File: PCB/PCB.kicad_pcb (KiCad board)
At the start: 2 copper layers, 3 parts, among them SW9 SW1_Push, U4 ER_OLEDM0.91_1x-I2C, U5 MOUDLE-SEEEDUINO-XIAO

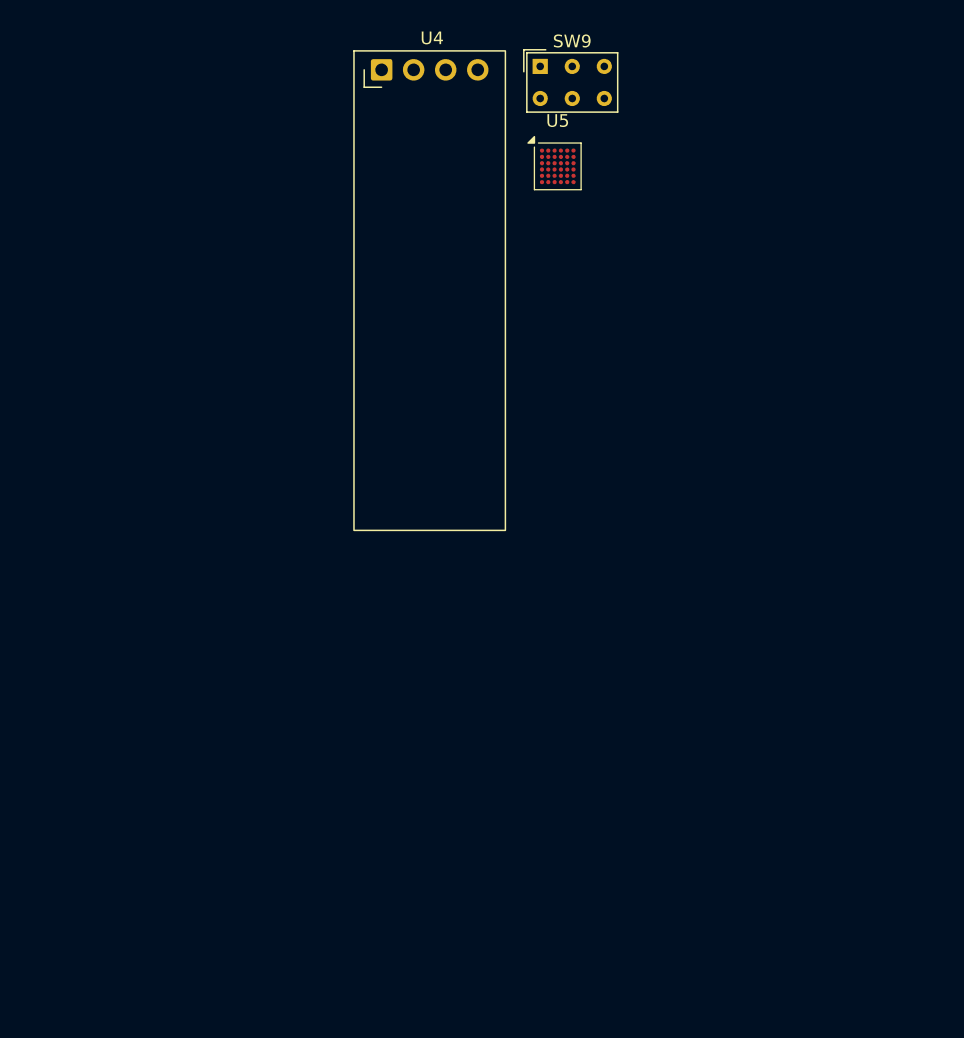
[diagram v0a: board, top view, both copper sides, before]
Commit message: Add Hakin Pad schematic image
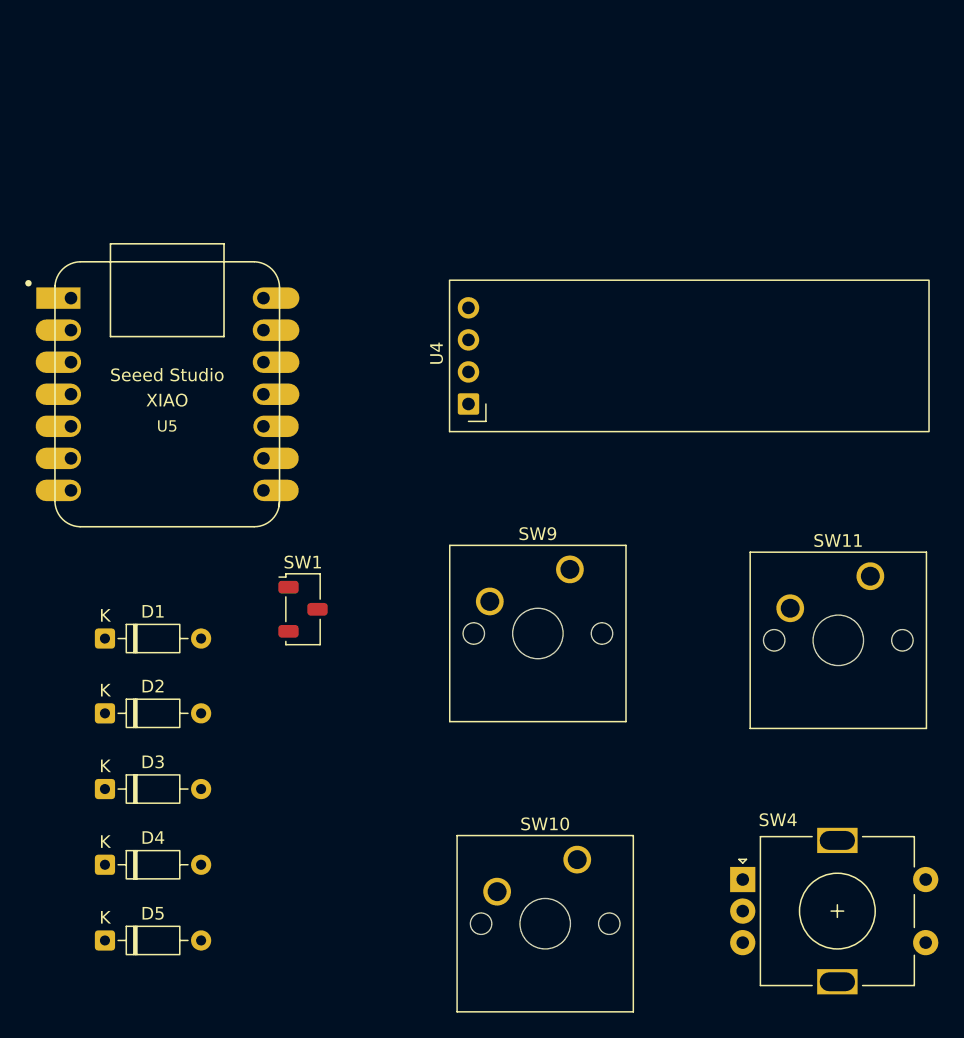
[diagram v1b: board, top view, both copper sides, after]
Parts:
- added D1: 1N4148, Diode_THT:D_DO-35_SOD27_P7.62mm_Horizontal, F.Cu at (108.5, 106.6)
- added D2: 1N4148, Diode_THT:D_DO-35_SOD27_P7.62mm_Horizontal, F.Cu at (108.5, 112.5)
- added D3: 1N4148, Diode_THT:D_DO-35_SOD27_P7.62mm_Horizontal, F.Cu at (108.5, 118.5)
- added D4: 1N4148, Diode_THT:D_DO-35_SOD27_P7.62mm_Horizontal, F.Cu at (108.5, 124.5)
- added D5: 1N4148, Diode_THT:D_DO-35_SOD27_P7.62mm_Horizontal, F.Cu at (108.5, 130.5)
- added SW1: SW4_Push, Button_Switch_SMD:Nidec_Copal_CAS-120A, F.Cu at (124.2, 104.2)
- added SW10: SW2_Push, Button_Switch_Keyboard:SW_Cherry_MX_1.00u_PCB, F.Cu at (145.9, 124.1)
- added SW11: SW3_Push, Button_Switch_Keyboard:SW_Cherry_MX_1.00u_PCB, F.Cu at (169.1, 101.6)
- added SW4: RotaryEncoder_Switch, Rotary_Encoder:RotaryEncoder_Alps_EC11E-Switch_Vertical_H20mm, F.Cu at (159.0, 125.7)
- SW9: footprint Button_Switch_THT:SW_NKK_GW12LJP -> Button_Switch_Keyboard:SW_Cherry_MX_1.00u_PCB
- U5: footprint Package_BGA:XFBGA-36_3.5x3.5mm_Layout6x6_P0.5mm -> footprints:XIAO-Generic-Hybrid-14P-2.54-21X17.8MM
- moved SW9 39.9 mm to (145.3, 101.1)
- moved U5 35.8 mm to (113.4, 87.2)
- moved U4 27.4 mm to (137.3, 88.0), turned to 90 degrees
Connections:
- SW9 pad 1: GND -> Net-(D1-A)
- U4 pad 4: Net-(U4-SDA) -> Net-(U4-SCL)
